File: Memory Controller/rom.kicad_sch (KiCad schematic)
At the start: 4 parts, among them U12 SST39SF010, U13 SST39SF010

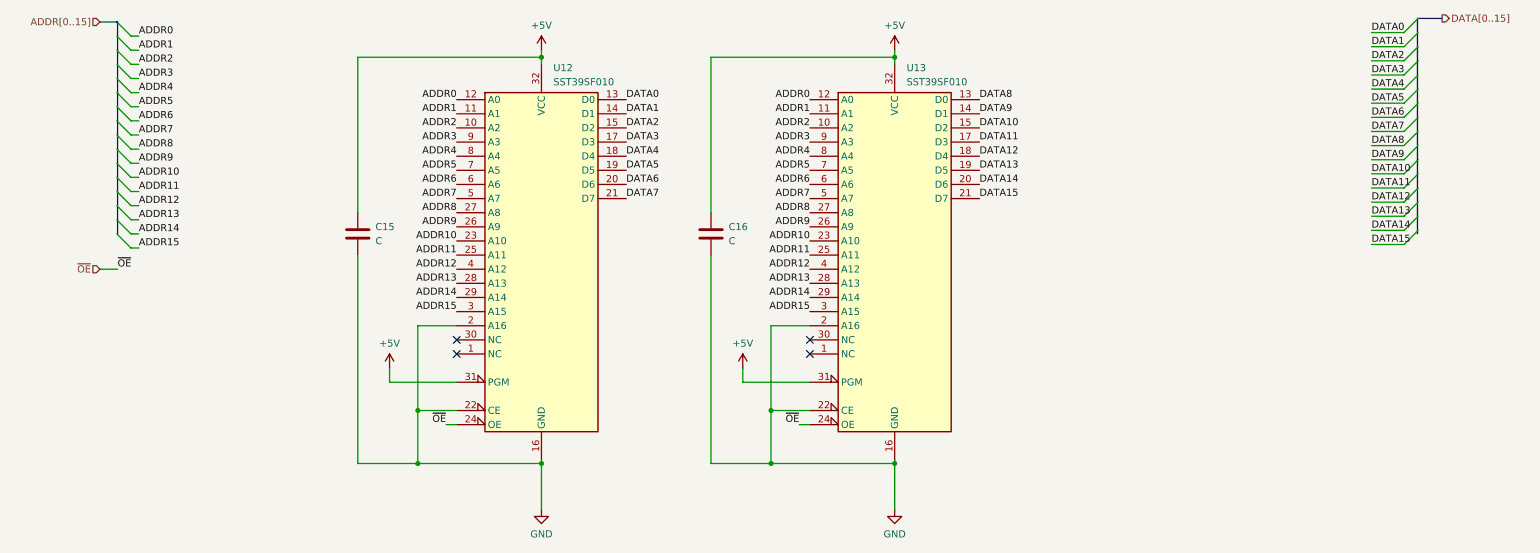
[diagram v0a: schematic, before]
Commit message: Memory Controller fabrication checks complete
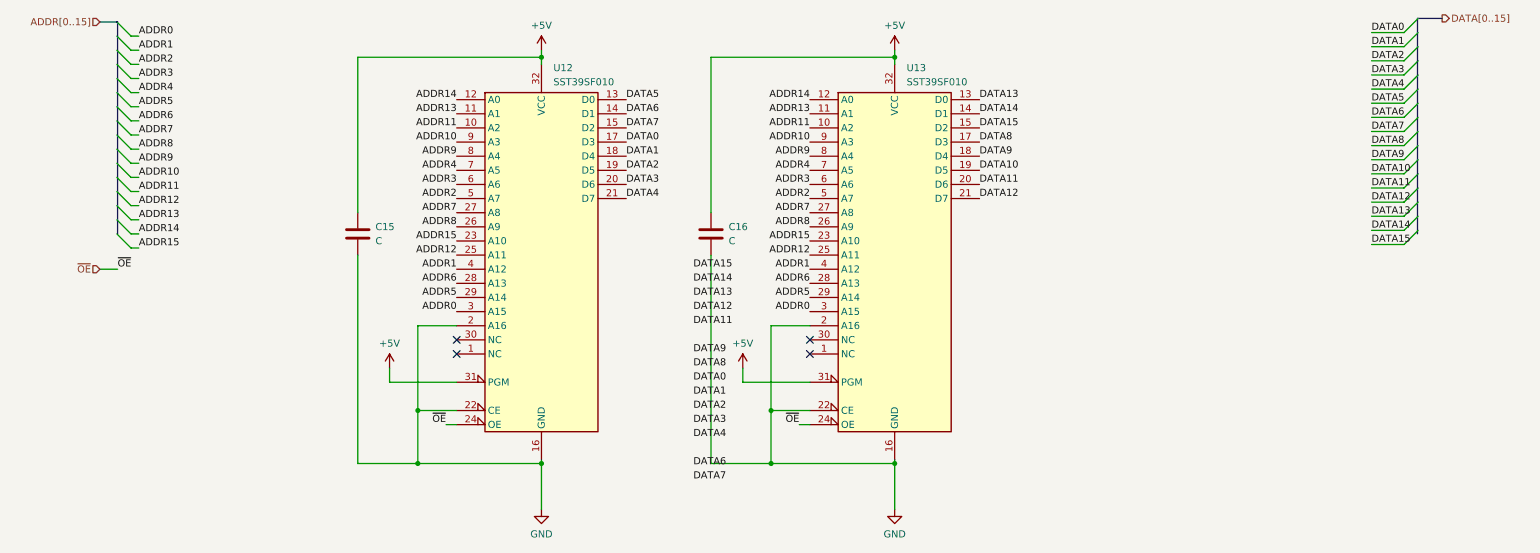
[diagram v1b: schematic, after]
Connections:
- net ADDR0: now also U12.3 (A15), U13.3 (A15); no longer U12.12 (A0), U13.12 (A0)
- net ADDR1: now also U12.4 (A12), U13.4 (A12); no longer U12.11 (A1), U13.11 (A1)
- net ADDR10: now also U12.9 (A3), U13.9 (A3); no longer U12.23 (A10), U13.23 (A10)
- net ADDR11: now also U12.10 (A2), U13.10 (A2); no longer U12.25 (A11), U13.25 (A11)
- net ADDR12: now also U12.25 (A11), U13.25 (A11); no longer U12.4 (A12), U13.4 (A12)
- net ADDR13: now also U12.11 (A1), U13.11 (A1); no longer U12.28 (A13), U13.28 (A13)
- net ADDR14: now also U12.12 (A0), U13.12 (A0); no longer U12.29 (A14), U13.29 (A14)
- net ADDR15: now also U12.23 (A10), U13.23 (A10); no longer U12.3 (A15), U13.3 (A15)
- net ADDR2: now also U12.5 (A7), U13.5 (A7); no longer U12.10 (A2), U13.10 (A2)
- net ADDR3: now also U12.6 (A6), U13.6 (A6); no longer U12.9 (A3), U13.9 (A3)
- net ADDR4: now also U12.7 (A5), U13.7 (A5); no longer U12.8 (A4), U13.8 (A4)
- net ADDR5: now also U12.29 (A14), U13.29 (A14); no longer U12.7 (A5), U13.7 (A5)
- net ADDR6: now also U12.28 (A13), U13.28 (A13); no longer U12.6 (A6), U13.6 (A6)
- net ADDR7: now also U12.27 (A8), U13.27 (A8); no longer U12.5 (A7), U13.5 (A7)
- net ADDR8: now also U12.26 (A9), U13.26 (A9); no longer U12.27 (A8), U13.27 (A8)
- net ADDR9: now also U12.8 (A4), U13.8 (A4); no longer U12.26 (A9), U13.26 (A9)
- net DATA0: now also U12.17 (D3); no longer U12.13 (D0)
- net DATA1: now also U12.18 (D4); no longer U12.14 (D1)
- net DATA10: now also U13.19 (D5); no longer U13.15 (D2)
- net DATA11: now also U13.20 (D6); no longer U13.17 (D3)
- net DATA12: now also U13.21 (D7); no longer U13.18 (D4)
- net DATA13: now also U13.13 (D0); no longer U13.19 (D5)
- net DATA14: now also U13.14 (D1); no longer U13.20 (D6)
- net DATA15: now also U13.15 (D2); no longer U13.21 (D7)
- net DATA2: now also U12.19 (D5); no longer U12.15 (D2)
- net DATA3: now also U12.20 (D6); no longer U12.17 (D3)
- net DATA4: now also U12.21 (D7); no longer U12.18 (D4)
- net DATA5: now also U12.13 (D0); no longer U12.19 (D5)
- net DATA6: now also U12.14 (D1); no longer U12.20 (D6)
- net DATA7: now also U12.15 (D2); no longer U12.21 (D7)
- net DATA8: now also U13.17 (D3); no longer U13.13 (D0)
- net DATA9: now also U13.18 (D4); no longer U13.14 (D1)
